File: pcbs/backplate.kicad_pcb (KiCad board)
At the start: 2 copper layers, 133.8 x 91.7 mm, 5 parts

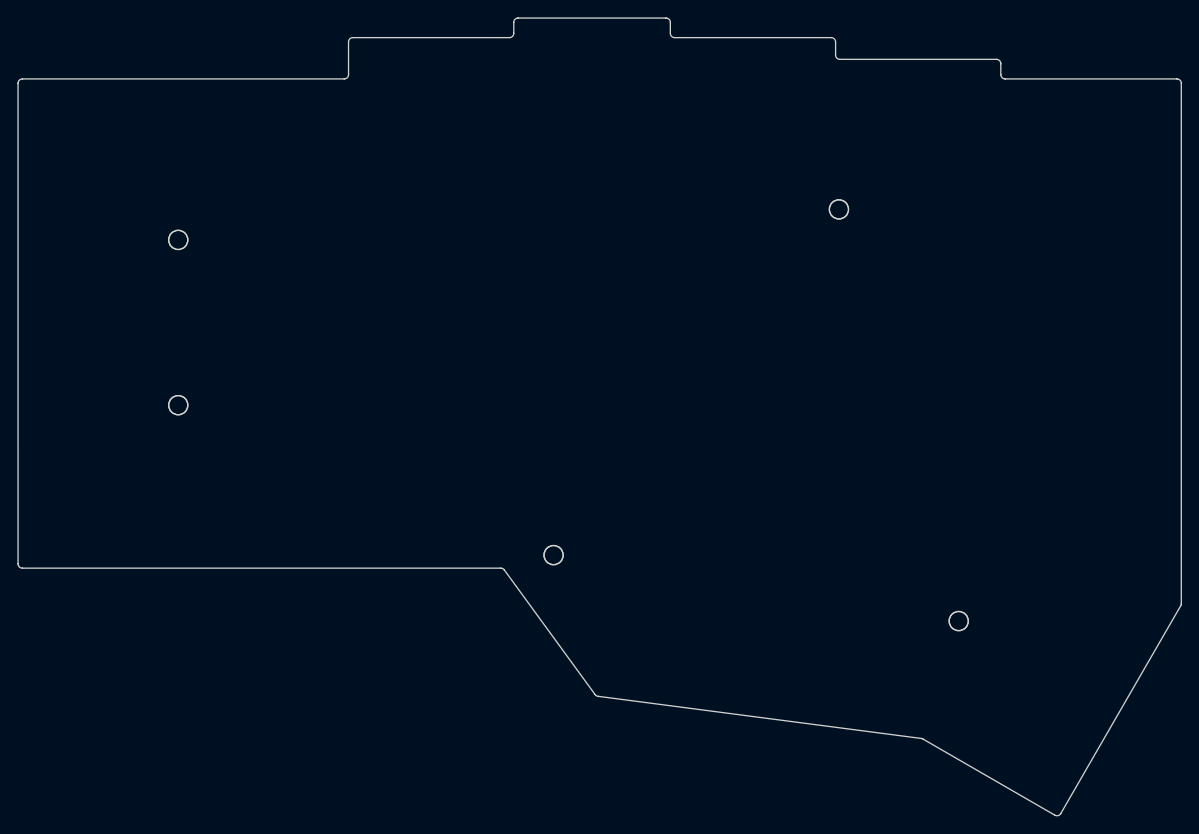
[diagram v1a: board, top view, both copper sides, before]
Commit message: build: generate PCB layouts, routing, gerbers, and preview images
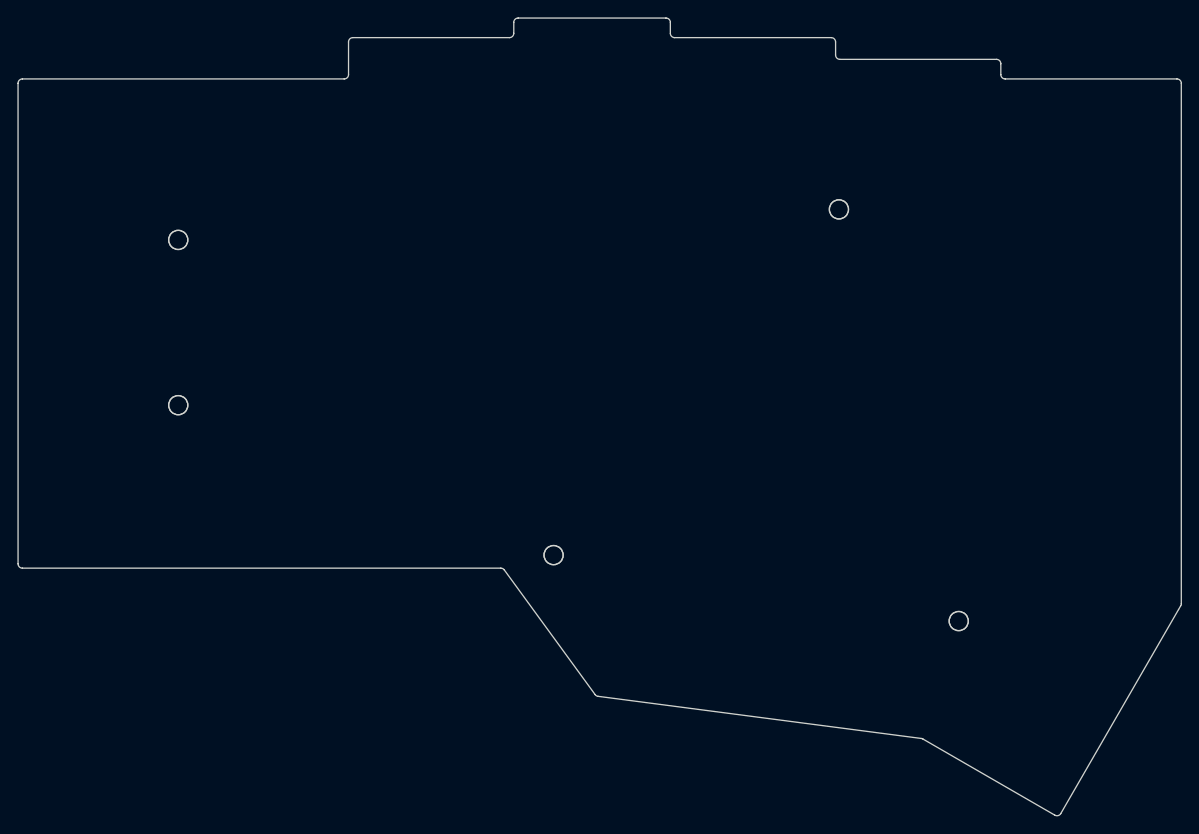
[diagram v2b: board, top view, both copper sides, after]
